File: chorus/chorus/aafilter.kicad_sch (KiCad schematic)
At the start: 7 parts

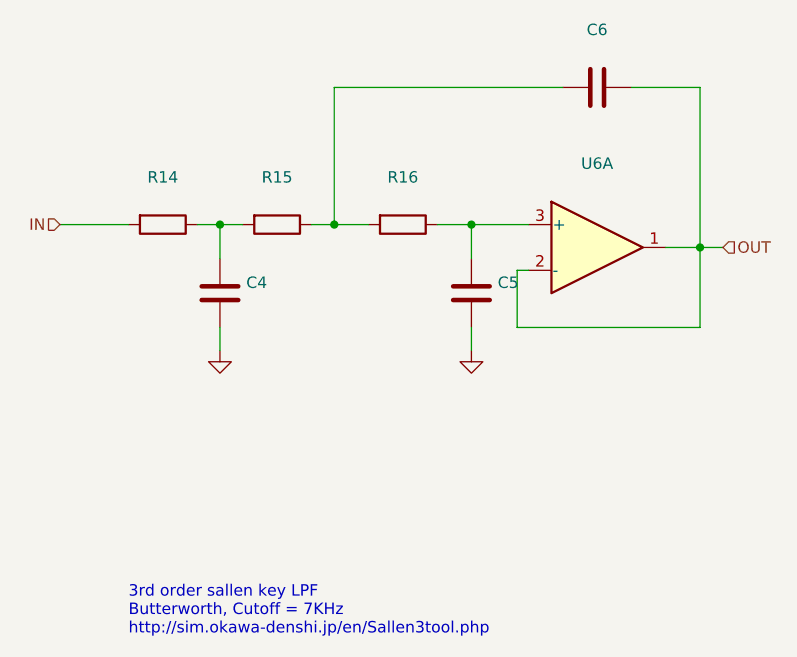
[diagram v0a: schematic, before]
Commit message: add output buffer
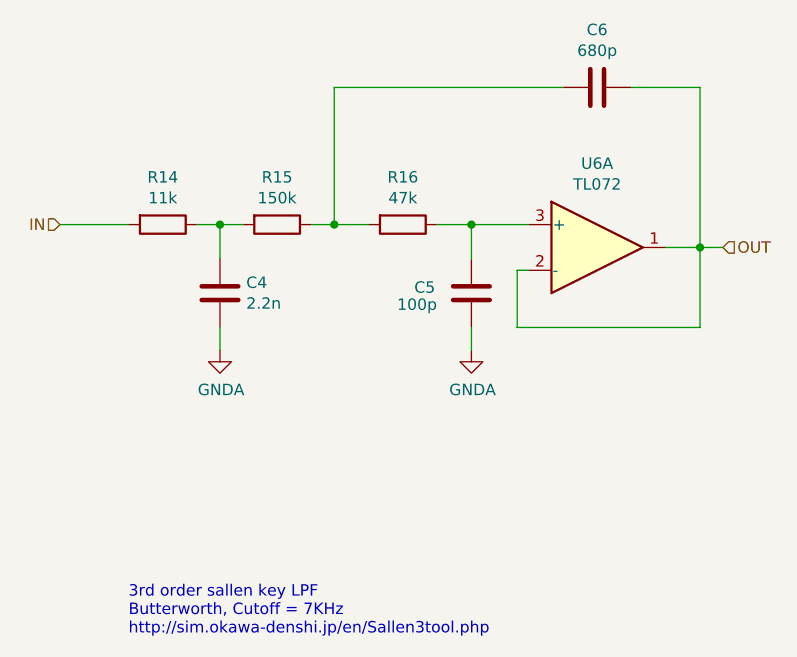
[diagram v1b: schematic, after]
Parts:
- C4: value (none) -> 2.2n
- C5: value (none) -> 100p
- C6: value (none) -> 680p
- R14: value (none) -> 11k
- R15: value (none) -> 150k
- R16: value (none) -> 47k
- U6: value (none) -> TL072
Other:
- company: (none) -> rabidaudio
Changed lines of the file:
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@@
 (kicad_sch (version 20211123) (generator eeschema)
   (paper "A4")
+  (title_block
+    (company "rabidaudio")
+  )
   (junction (at 107.95 93.98) (diameter 0) (color 0 0 0 0)
   )
@@
     (in_bom yes) (on_board yes)
     (property "Reference" "R16" (id 0) (at 115.57 88.7222 90))
-    (property "Value" "" (id 1) (at 115.57 91.0336 90))
+    (property "Value" "47k" (id 1) (at 115.57 91.0336 90))
     (property "Footprint" "kicad-legacy/kicad-footprints/Resistor_THT.pretty:R_Axial_DIN0204_L3.6mm_D1.6mm_P2.54mm_Vertical" (id 2) (at 115.57 92.202 90)
       (effects (font (size 1.27 1.27)) hide)
@@
   (symbol (lib_id "power:GNDA") (at 123.19 107.95 0) (unit 1)
     (in_bom yes) (on_board yes)
-    (property "Reference" "#PWR?" (id 0) (at 123.19 114.3 0)
-      (effects (font (size 1.27 1.27)) hide)
-    )
-    (property "Value" "" (id 1) (at 123.317 112.3442 0))
+    (property "Reference" "#PWR0106" (id 0) (at 123.19 114.3 0)
+      (effects (font (size 1.27 1.27)) hide)
+    )
+    (property "Value" "GNDA" (id 1) (at 123.317 112.3442 0))
     (property "Footprint" "" (id 2) (at 123.19 107.95 0)
       (effects (font (size 1.27 1.27)) hide)
@@
       (effects (font (size 1.27 1.27)) (justify right))
     )
-    (property "Value" "" (id 1) (at 98.171 102.743 0)
+    (property "Value" "2.2n" (id 1) (at 98.171 102.743 0)
       (effects (font (size 1.27 1.27)) (justify right))
     )
@@
     (in_bom yes) (on_board yes)
     (property "Reference" "U6" (id 0) (at 137.16 87.1982 0))
-    (property "Value" "" (id 1) (at 137.16 89.5096 0))
+    (property "Value" "TL072" (id 1) (at 137.16 89.5096 0))
     (property "Footprint" "kicad-legacy/Housings_DIP.pretty:DIP-8_W7.62mm" (id 2) (at 137.16 96.52 0)
       (effects (font (size 1.27 1.27)) hide)
@@
     (in_bom yes) (on_board yes)
     (property "Reference" "R15" (id 0) (at 101.6 88.7222 90))
-    (property "Value" "" (id 1) (at 101.6 91.0336 90))
+    (property "Value" "150k" (id 1) (at 101.6 91.0336 90))
     (property "Footprint" "kicad-legacy/kicad-footprints/Resistor_THT.pretty:R_Axial_DIN0204_L3.6mm_D1.6mm_P2.54mm_Vertical" (id 2) (at 101.6 92.202 90)
       (effects (font (size 1.27 1.27)) hide)
@@
   (symbol (lib_id "power:GNDA") (at 95.25 107.95 0) (unit 1)
     (in_bom yes) (on_board yes)
-    (property "Reference" "#PWR?" (id 0) (at 95.25 114.3 0)
-      (effects (font (size 1.27 1.27)) hide)
-    )
-    (property "Value" "" (id 1) (at 95.377 112.3442 0))
+    (property "Reference" "#PWR0103" (id 0) (at 95.25 114.3 0)
+      (effects (font (size 1.27 1.27)) hide)
+    )
+    (property "Value" "GNDA" (id 1) (at 95.377 112.3442 0))
     (property "Footprint" "" (id 2) (at 95.25 107.95 0)
       (effects (font (size 1.27 1.27)) hide)
@@
   (symbol (lib_id "Device:C") (at 123.19 101.6 180) (unit 1)
     (in_bom yes) (on_board yes)
-    (property "Reference" "C5" (id 0) (at 126.111 100.4316 0)
-      (effects (font (size 1.27 1.27)) (justify right))
-    )
-    (property "Value" "" (id 1) (at 126.111 102.743 0)
+    (property "Reference" "C5" (id 0) (at 116.84 100.965 0)
+      (effects (font (size 1.27 1.27)) (justify right))
+    )
+    (property "Value" "100p" (id 1) (at 114.935 102.87 0)
       (effects (font (size 1.27 1.27)) (justify right))
     )
@@
     (in_bom yes) (on_board yes)
     (property "Reference" "C6" (id 0) (at 137.16 72.3392 90))
-    (property "Value" "" (id 1) (at 137.16 74.6506 90))
+    (property "Value" "680p" (id 1) (at 137.16 74.6506 90))
     (property "Footprint" "" (id 2) (at 133.35 79.7052 0)
       (effects (font (size 1.27 1.27)) hide)
@@
     (in_bom yes) (on_board yes)
     (property "Reference" "R14" (id 0) (at 88.9 88.7222 90))
-    (property "Value" "" (id 1) (at 88.9 91.0336 90))
+    (property "Value" "11k" (id 1) (at 88.9 91.0336 90))
     (property "Footprint" "kicad-legacy/kicad-footprints/Resistor_THT.pretty:R_Axial_DIN0204_L3.6mm_D1.6mm_P2.54mm_Vertical" (id 2) (at 88.9 92.202 90)
       (effects (font (size 1.27 1.27)) hide)
